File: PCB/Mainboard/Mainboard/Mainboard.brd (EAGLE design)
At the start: 150 x 60 mm, 18 parts

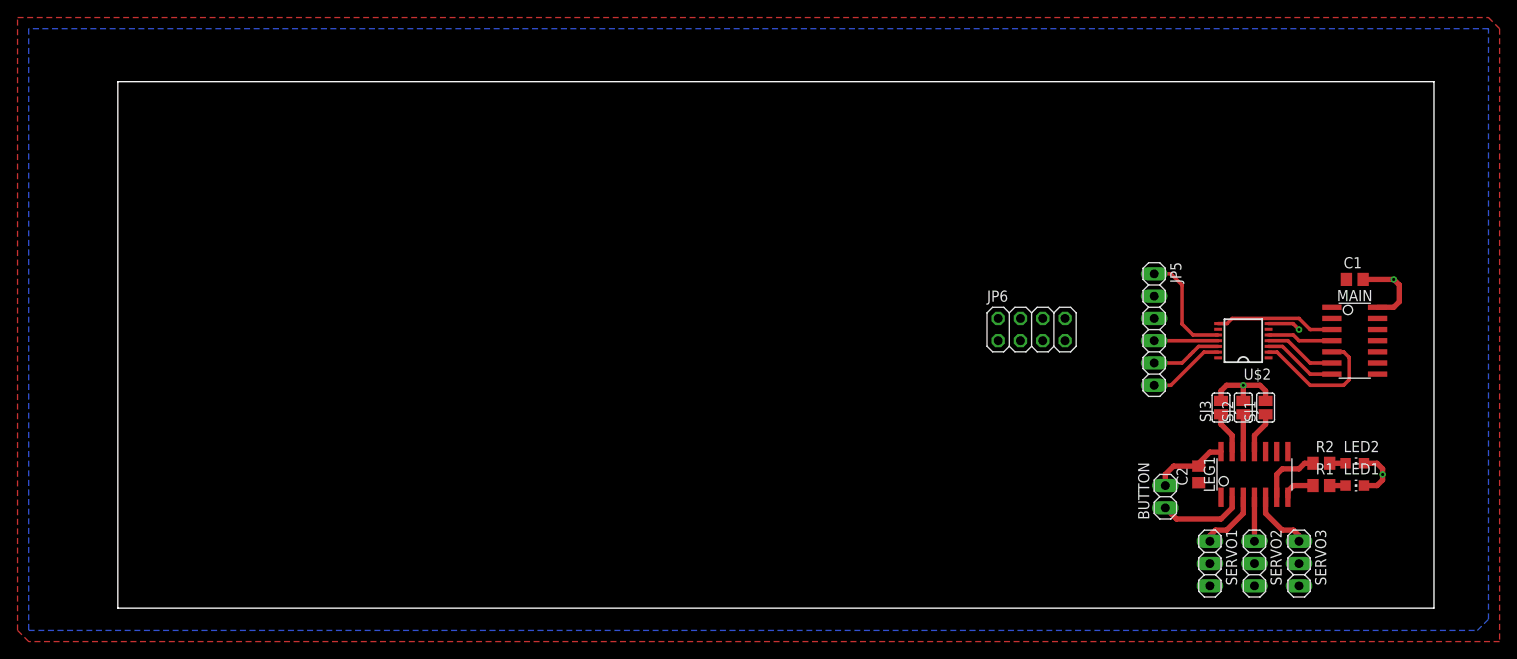
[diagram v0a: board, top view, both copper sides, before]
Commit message: Added missing leg controller +  layout
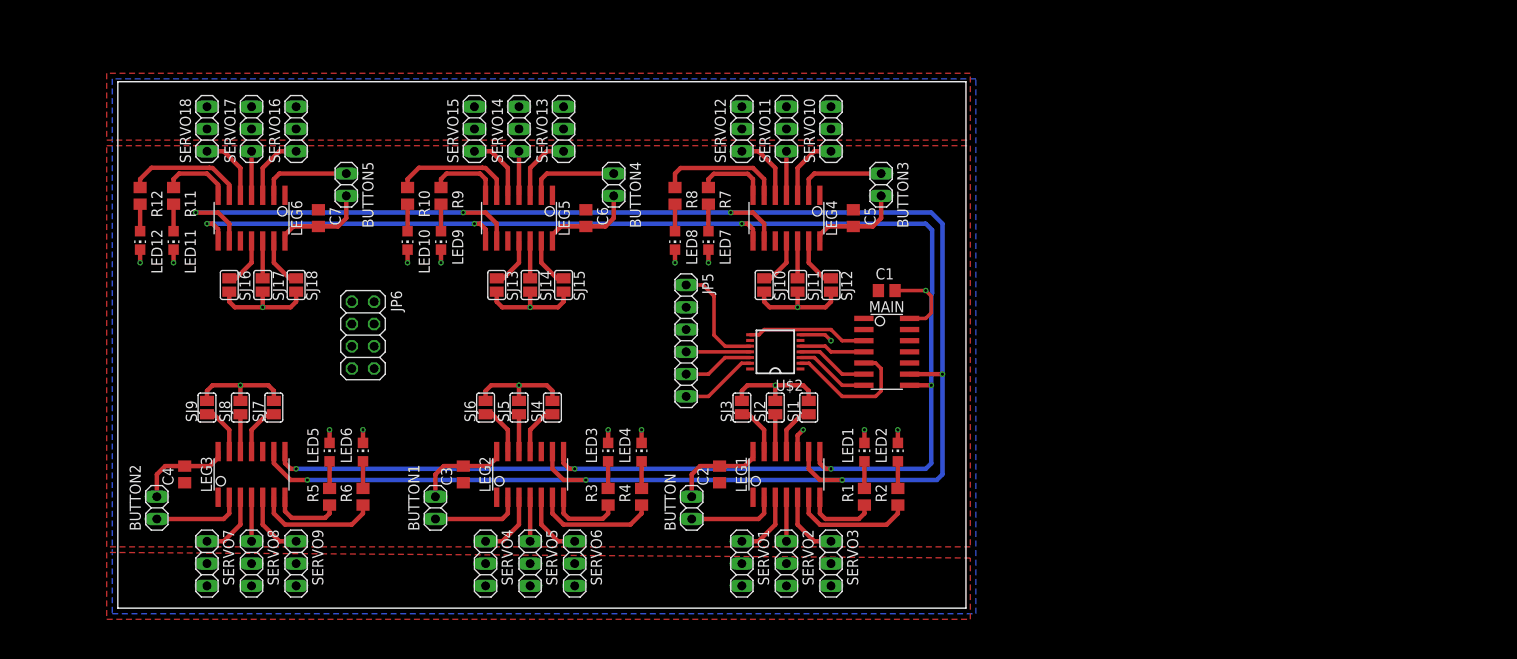
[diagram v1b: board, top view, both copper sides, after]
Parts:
- added BUTTON1, BUTTON2, BUTTON3, BUTTON4, BUTTON5: (no value), pinhead:1X02
- added C3, C4, C5, C6, C7: (no value), rcl:C0805
- added LED10, LED11, LED12, LED3, LED4, LED5, LED6, LED7, LED8, LED9: (no value), led:CHIP-LED0805
- added LEG2, LEG3, LEG4, LEG5, LEG6: ATTINY1614, ATTINY1614:SOIC14
- added R10, R11, R12, R3, R4, R5, R6, R7, R8, R9: (no value), rcl:R0805
- added SERVO10, SERVO11, SERVO12, SERVO13, SERVO14, SERVO15, SERVO16, SERVO17, SERVO18, SERVO4, SERVO5, SERVO6, SERVO7, SERVO8, SERVO9: (no value), pinhead:1X03
- added SJ10, SJ11, SJ12, SJ13, SJ14, SJ15, SJ16, SJ17, SJ18, SJ4, SJ5, SJ6, SJ7, SJ8, SJ9: (no value), jumper:SJ
- moved JP6 76.2 mm to (27.9, 31.1), turned to 270 degrees
- moved LED1 56.0 mm to (85.1, 17.8), turned to 0 degrees
- moved C2 54.6 mm to (68.6, 15.2)
- moved SJ3 54.6 mm to (71.1, 22.9)
- moved BUTTON 54.0 mm to (65.4, 11.4)
- moved C1 53.4 mm to (87.6, 36.2)
- moved JP5 53.4 mm to (64.8, 30.5)
- moved MAIN 53.4 mm to (87.6, 29.2)
- moved U$2 53.4 mm to (74.9, 29.2)
- moved SERVO3 53.3 mm to (81.3, 5.08)
- moved SJ2 53.3 mm to (74.9, 22.9)
- moved LEG1 53.3 mm to (76.2, 15.2)
- moved SERVO1 53.3 mm to (71.1, 5.08)
- moved SERVO2 53.3 mm to (76.2, 5.08)
- moved LED2 52.1 mm to (88.9, 17.8), turned to 0 degrees
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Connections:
- net ADDR0 renamed N$3
- net ADDR1 renamed N$4
- net ADDR2 renamed N$5
- net BTN renamed N$8
- net LED1 renamed N$1
- net LED2 renamed N$2
- net S1 renamed N$9
- net S2 renamed N$10
- net S3 renamed N$12
- removed net N$16: JP6.5
- removed net N$17: JP6.7
- removed net N$18: JP6.2
- removed net N$19: JP6.4
- removed net N$20: JP6.6
- removed net N$21: JP6.8
- new net N$11: LED3.A, R3.2
- new net N$13: LED4.A, R4.2
- new net N$14: LEG2.7, R3.1
- new net N$15: LEG2.6, R4.1
- new net N$22: LEG2.11, SJ4.1
- new net N$23: LEG2.12, SJ5.1
- new net N$24: LEG2.13, SJ6.1
- new net N$25: BUTTON1.1, LEG2.2
- new net N$26: LEG2.3, SERVO4.1
- new net N$27: LEG2.4, SERVO5.1
- new net N$28: LEG2.5, SERVO6.1
- new net N$29: LED5.A, R5.2
- new net N$30: LED6.A, R6.2
- new net N$31: LEG3.7, R5.1
- new net N$32: LEG3.6, R6.1
- new net N$33: LEG3.11, SJ7.1
- new net N$34: LEG3.12, SJ8.1
- new net N$35: LEG3.13, SJ9.1
- new net N$36: BUTTON2.1, LEG3.2
- new net N$37: LEG3.3, SERVO7.1
- new net N$38: LEG3.4, SERVO8.1
- new net N$39: LEG3.5, SERVO9.1
- new net N$40: LED7.A, R7.2
- new net N$41: LED8.A, R8.2
- new net N$42: LEG4.7, R7.1
- new net N$43: LEG4.6, R8.1
- new net N$44: LEG4.11, SJ10.1
- new net N$45: LEG4.12, SJ11.1
- new net N$46: LEG4.13, SJ12.1
- new net N$47: BUTTON3.1, LEG4.2
- new net N$48: LEG4.3, SERVO10.1
- new net N$49: LEG4.4, SERVO11.1
- new net N$50: LEG4.5, SERVO12.1
- new net N$51: LED9.A, R9.2
- new net N$52: LED10.A, R10.2
- new net N$53: LEG5.7, R9.1
- new net N$54: LEG5.6, R10.1
- new net N$55: LEG5.11, SJ13.1
- new net N$56: LEG5.12, SJ14.1
- new net N$57: LEG5.13, SJ15.1
- new net N$58: BUTTON4.1, LEG5.2
- new net N$59: LEG5.3, SERVO13.1
- new net N$60: LEG5.4, SERVO14.1
- new net N$61: LEG5.5, SERVO15.1
- new net N$62: LED11.A, R11.2
- new net N$63: LED12.A, R12.2
- new net N$64: LEG6.7, R11.1
- new net N$65: LEG6.6, R12.1
- new net N$66: LEG6.11, SJ16.1
- new net N$67: LEG6.12, SJ17.1
- new net N$68: LEG6.13, SJ18.1
- new net N$69: BUTTON5.1, LEG6.2
- new net N$70: LEG6.3, SERVO16.1
- new net N$71: LEG6.4, SERVO17.1
- new net N$72: LEG6.5, SERVO18.1
- new net UPDI2: JP6.5, LEG2.10
- new net UPDI3: JP6.7, LEG3.10
- new net UPDI4: JP6.4, LEG4.10
- new net UPDI5: JP6.6, LEG5.10
- new net UPDI6: JP6.8, LEG6.10
- new net VCC/2: SERVO10.2, SERVO11.2, SERVO12.2, SERVO13.2, SERVO14.2, SERVO15.2, SERVO16.2, SERVO17.2, SERVO18.2
- net +5V: now also C3.1, C4.1, C5.1, C6.1, C7.1, LEG2.1, LEG3.1, LEG4.1, LEG5.1, LEG6.1
- net GND: now also BUTTON1.2, BUTTON2.2, BUTTON3.2, BUTTON4.2, BUTTON5.2, C3.2, C4.2, C5.2, C6.2, C7.2, JP6.2, LED10.C, LED11.C, LED12.C, LED3.C, LED4.C, LED5.C, LED6.C, LED7.C, LED8.C, LED9.C, LEG2.14, LEG3.14, LEG4.14, LEG5.14, LEG6.14, SERVO10.3, SERVO11.3, SERVO12.3, SERVO13.3, SERVO14.3, SERVO15.3, SERVO16.3, SERVO17.3, SERVO18.3, SERVO4.3, SERVO5.3, SERVO6.3, SERVO7.3, SERVO8.3, SERVO9.3, SJ10.2, SJ11.2, SJ12.2, SJ13.2, SJ14.2, SJ15.2, SJ16.2, SJ17.2, SJ18.2, SJ4.2, SJ5.2, SJ6.2, SJ7.2, SJ8.2, SJ9.2
- net SCL: now also LEG2.9, LEG3.9, LEG4.9, LEG5.9, LEG6.9
- net SDA: now also LEG2.8, LEG3.8, LEG4.8, LEG5.8, LEG6.8
- net VCC: now also SERVO4.2, SERVO5.2, SERVO6.2, SERVO7.2, SERVO8.2, SERVO9.2
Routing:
- net SCL: track 0.00 -> 228.0 mm, vias 0 -> 7
- net SDA: track 0.00 -> 201.9 mm, vias 0 -> 7
- net GND: track 37.4 -> 170.5 mm, vias 4 -> 20
- net N$43: track 0.00 -> 14.4 mm
- net N$54: track 0.00 -> 14.0 mm
- net N$32: track 0.00 -> 14.0 mm
- net N$15: track 0.00 -> 14.0 mm
- net N$65: track 0.00 -> 13.7 mm
- net N$47: track 0.00 -> 10.4 mm
- net N$69: track 0.00 -> 10.4 mm
- net N$58: track 0.00 -> 10.4 mm
- net N$25: track 0.00 -> 10.4 mm
- net N$36: track 0.00 -> 10.4 mm
- net N$53: track 0.00 -> 8.40 mm
- net N$42: track 0.00 -> 8.38 mm
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- added copper zone on layer 1, net VCC
- added copper zone on layer 1, net VCC/2
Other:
- board size 150 x 60 mm -> 96.7 x 60 mm

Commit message: Finished layout for current circuit
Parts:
- added R13, R14: (no value), rcl:R0805
- SJ1, SJ10, SJ11, SJ12, SJ13, SJ14, SJ15, SJ16, SJ17, SJ18, SJ2, SJ3, SJ4, SJ5, SJ6, SJ7, SJ8, SJ9: device jumper:SJ -> rcl:R0402
- moved SJ16 8.98 mm to (21.6, 38.1)
- moved SJ9 8.98 mm to (19.1, 21.6)
- moved JP6 8.91 mm to (36.8, 30.5)
- moved R12 7.65 mm to (10.2, 46.4)
- moved C4 7.62 mm to (15.2, 15.2)
- moved LED12 7.62 mm to (10.2, 41.9)
- moved BUTTON2 7.62 mm to (12.1, 11.4)
- moved SJ13 6.48 mm to (49.5, 38.1)
- moved SJ8 6.48 mm to (20.3, 21.6)
- moved SJ17 6.48 mm to (22.9, 38.1)
- moved R11 6.38 mm to (12.7, 46.4)
- moved R5 6.38 mm to (30.5, 13.3)
- moved JP5 6.38 mm to (58.4, 29.8)
- moved LED5 6.35 mm to (30.5, 17.8)
- moved SERVO16 6.35 mm to (26.7, 54.6)
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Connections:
- net +5V: now also R13.2, R14.2
- net SCL: now also R14.1
- net SDA: now also R13.1
- net UPDI0: now also JP6.6; no longer JP6.1
- net UPDI1: now also JP6.5; no longer JP6.3
- net UPDI2: now also JP6.8; no longer JP6.5
- net UPDI5: now also JP6.3; no longer JP6.6
- net UPDI6: now also JP6.1; no longer JP6.8
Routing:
- net UPDI0: track 0.00 -> 52.7 mm, vias 0 -> 1
- net UPDI1: track 2.74 -> 51.2 mm
- net UPDI4: track 0.00 -> 45.2 mm, vias 0 -> 1
- net GND: track 170.5 -> 144.2 mm, vias 20 -> 8
- net UPDI6: track 0.00 -> 21.5 mm, vias 0 -> 1
- net UPDI5: track 0.00 -> 20.6 mm, vias 0 -> 1
- net UPDI3: track 0.00 -> 20.4 mm, vias 0 -> 1
- net UPDI2: track 0.00 -> 20.4 mm, vias 0 -> 1
- net SDA: track 201.9 -> 192.2 mm
- net RXD_B: track 8.07 -> 17.2 mm
- net BRK_B: track 8.85 -> 18.0 mm
- net TXD_B: track 7.29 -> 16.4 mm
- net SCL: track 228.0 -> 219.7 mm
- net STATE_B: track 12.8 -> 20.3 mm
- net RXD_A: track 8.27 -> 5.21 mm
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
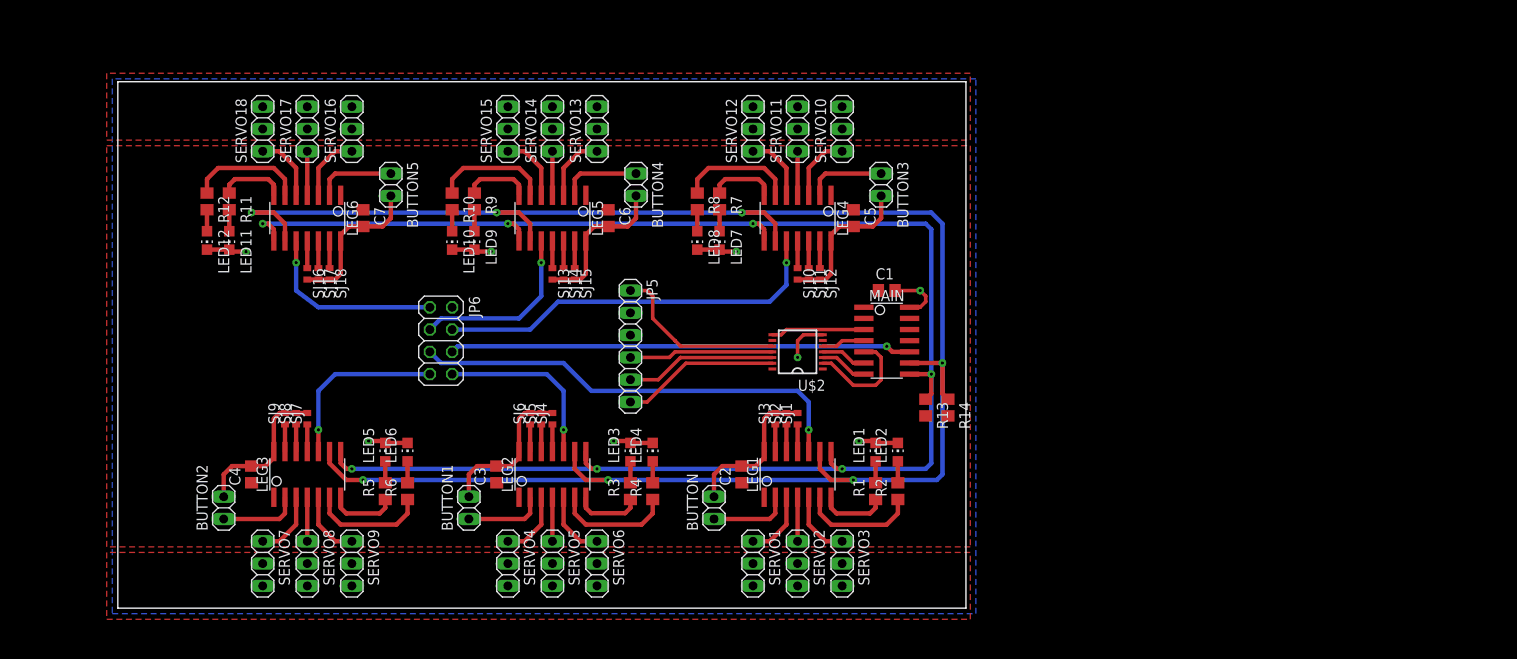
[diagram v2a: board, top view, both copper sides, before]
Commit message: Added 4 holes
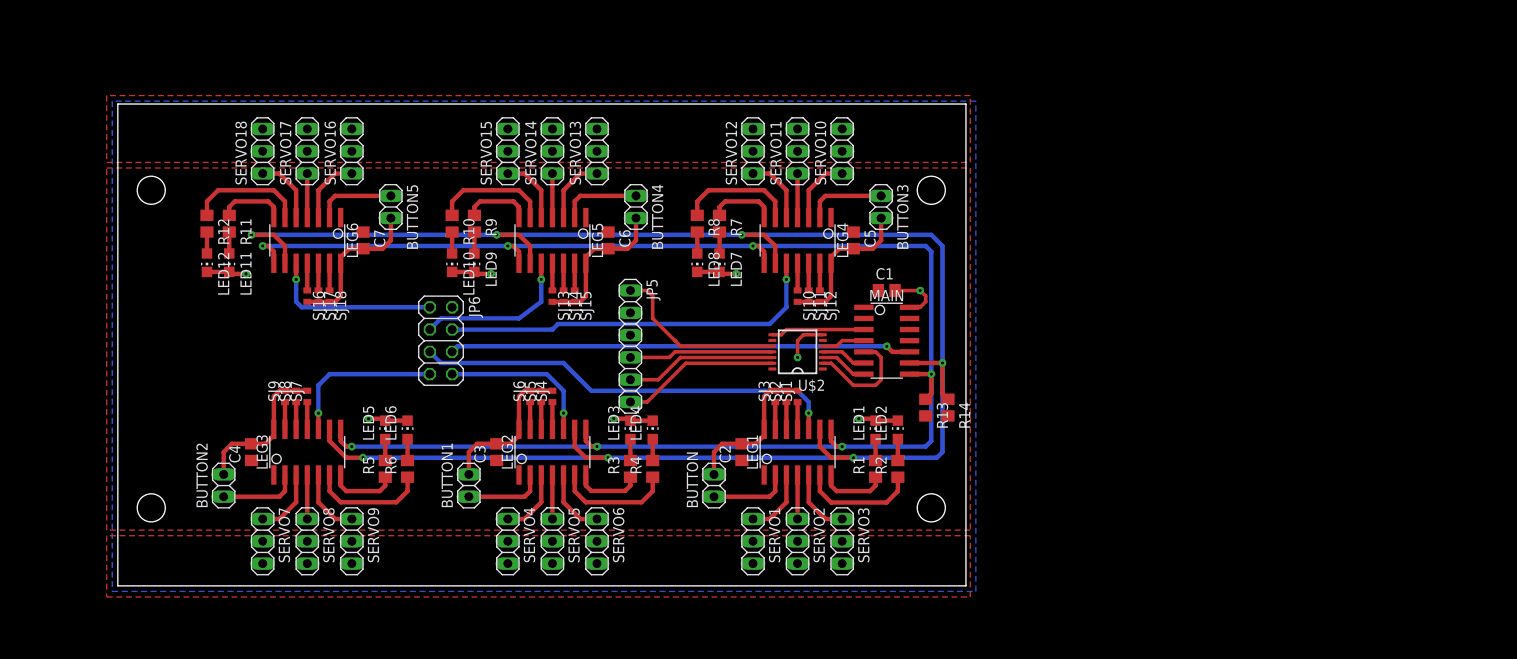
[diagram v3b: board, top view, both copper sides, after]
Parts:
- moved C5 2.54 mm to (83.8, 41.9)
- moved C6 2.54 mm to (55.9, 41.9)
- moved C7 2.54 mm to (27.9, 41.9)
- moved LEG4 2.54 mm to (77.5, 41.9)
- moved LEG5 2.54 mm to (49.5, 41.9)
- moved LEG6 2.54 mm to (21.6, 41.9)
- moved BUTTON 2.54 mm to (67.9, 14.0)
- moved BUTTON1 2.54 mm to (40.0, 14.0)
- moved BUTTON2 2.54 mm to (12.1, 14.0)
- moved C2 2.54 mm to (71.1, 17.8)
- moved C3 2.54 mm to (43.2, 17.8)
- moved C4 2.54 mm to (15.2, 17.8)
- moved LEG1 2.54 mm to (77.5, 17.8)
- moved LEG2 2.54 mm to (49.5, 17.8)
- moved LEG3 2.54 mm to (21.6, 17.8)
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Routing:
- net SCL: track 219.7 -> 214.7 mm
- net SDA: track 192.2 -> 187.2 mm
- net UPDI1: track 51.2 -> 48.7 mm
- net UPDI2: track 20.4 -> 17.9 mm
- net UPDI5: track 20.6 -> 18.2 mm
- net UPDI3: track 20.4 -> 18.2 mm
- net UPDI6: track 21.5 -> 19.9 mm
- net UPDI4: track 45.2 -> 44.2 mm
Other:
- board size 96.7 x 60 mm -> 96.7 x 54.9 mm
